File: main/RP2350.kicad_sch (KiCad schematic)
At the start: 26 parts, among them U1 RP2350_60QFN, U2 IC_ESPIF_ESP32-C3-MINI-1-N4

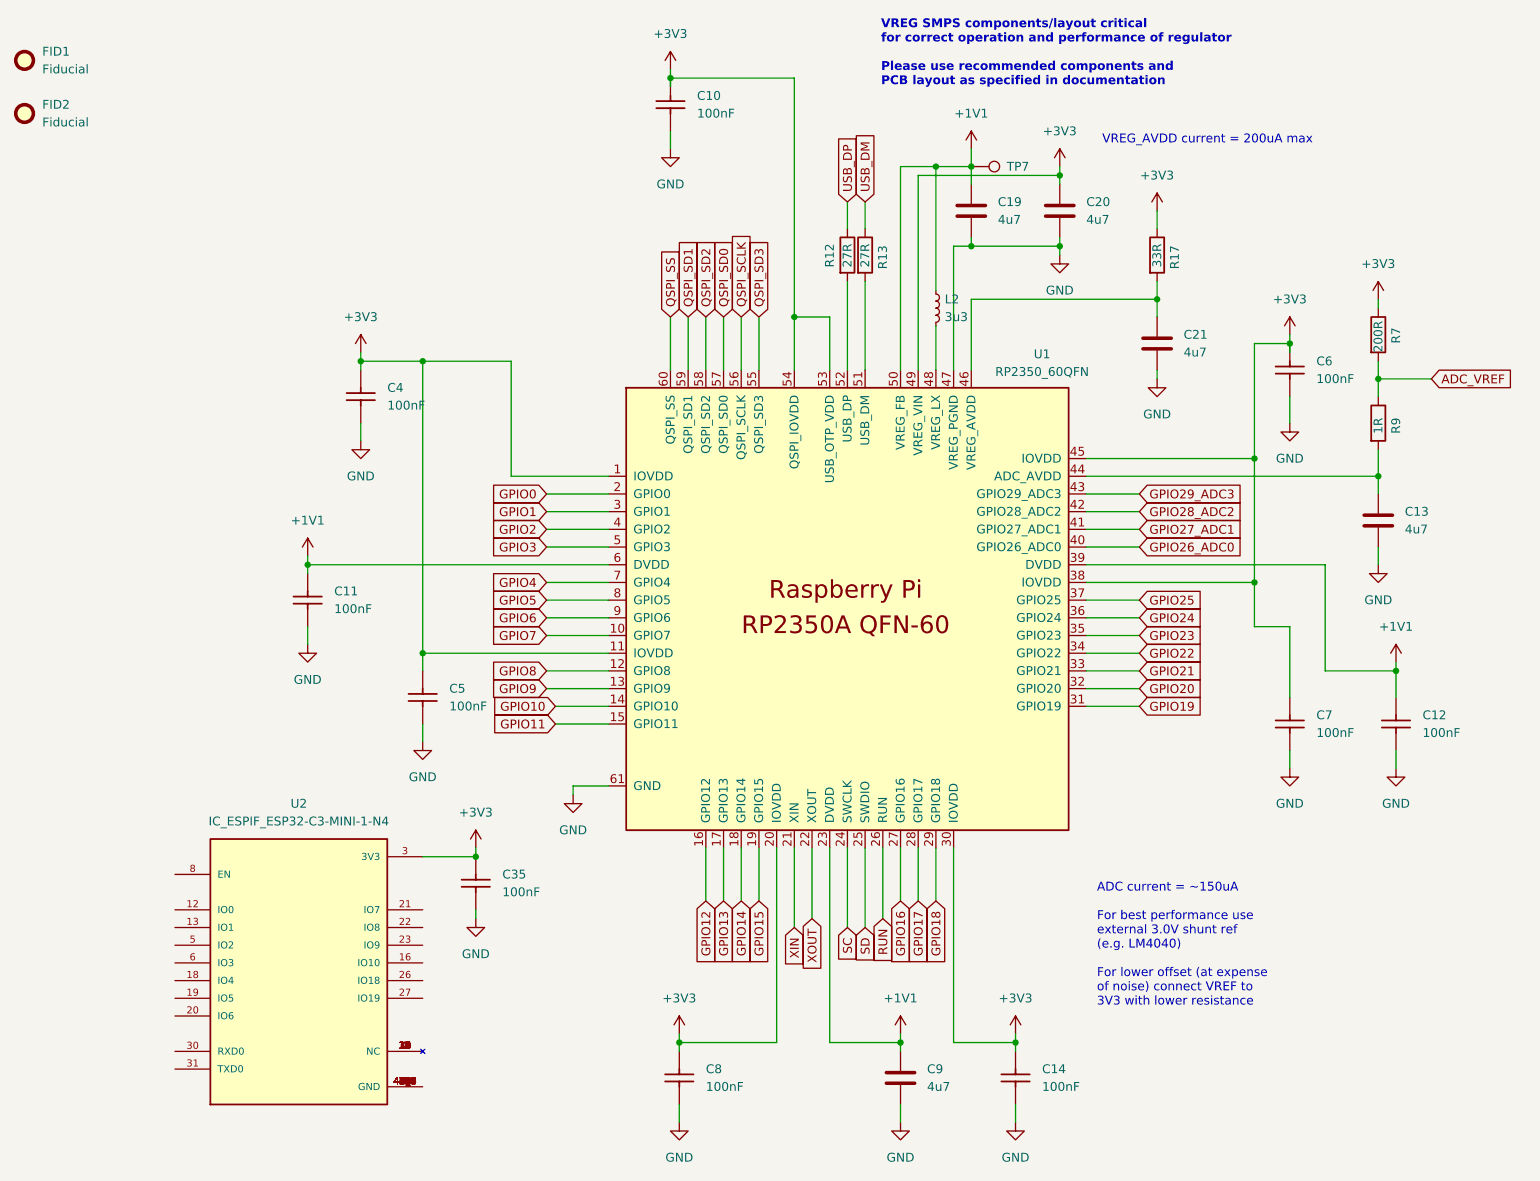
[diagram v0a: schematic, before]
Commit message: last commit with pi-pico still on
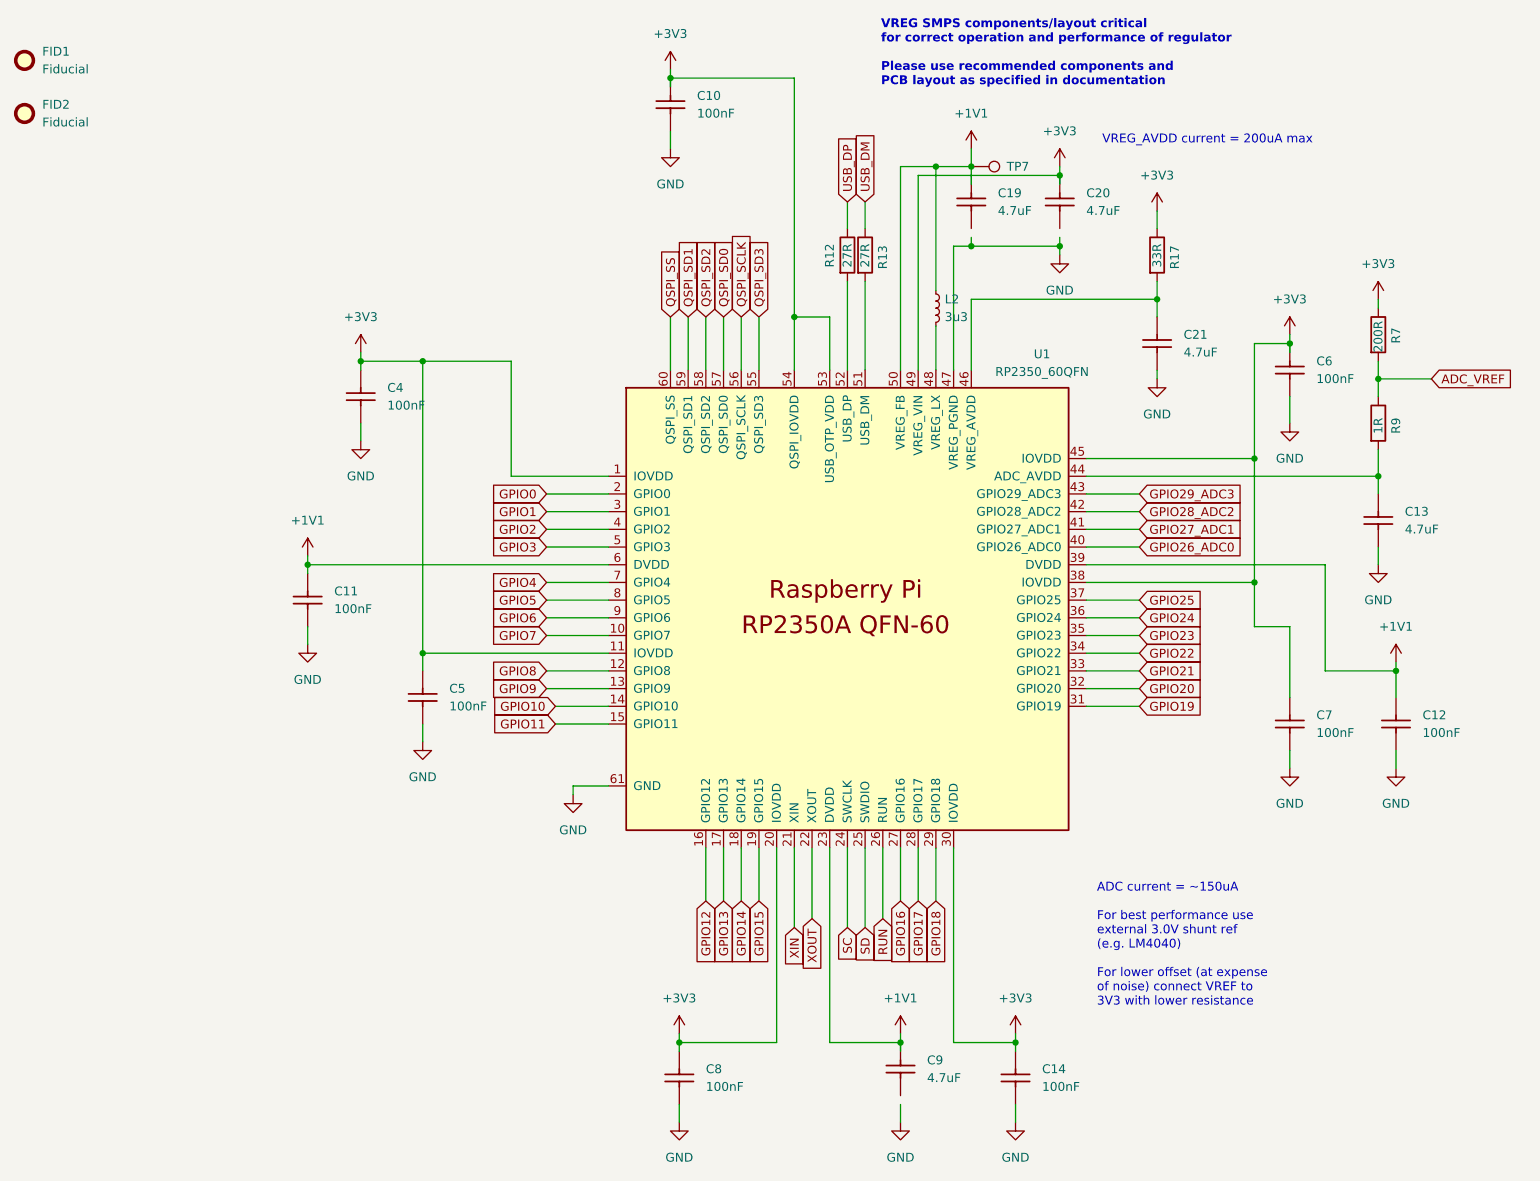
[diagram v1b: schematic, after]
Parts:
- removed C35: 100NF_0201_10V_X7R, smv_footprints:C_0201_0603Metric, symbol smv_capacitors:100NF_0201_10V_X7R
- removed U2: IC_ESPIF_ESP32-C3-MINI-1-N4, smv_footprints:IC_ESPIF_ESP32-C3-MINI-1-N4, symbol smv_ic:IC_ESPIF_ESP32-C3-MINI-1-N4
- C13, C19, C20, C21: value 4u7 -> 4.7UF 0402 10V X7R; footprint Capacitor_SMD:C_0402_1005Metric -> smv_footprints:C_0402_1005Metric; symbol Device:C -> smv_capacitors:4.7UF_0402_10V_X7R; Voltage (none) -> 0V; manf (none) -> Generic; manfn# (none) -> Generic; val (none) -> 4.7uF
- C9: value 4u7 -> 4.7UF 0402 10V X7R; footprint Capacitor_SMD:C_0201_0603Metric -> smv_footprints:C_0402_1005Metric; symbol Device:C -> smv_capacitors:4.7UF_0402_10V_X7R; Voltage (none) -> 0V; manf (none) -> Generic; manfn# (none) -> Generic; val (none) -> 4.7uF
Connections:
- net +1V1: no longer C19.1
- net GND: no longer C19.2, C20.2, C9.2
